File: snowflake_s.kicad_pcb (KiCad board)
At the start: 2 copper layers, 34.6 x 49.5 mm, 6 parts

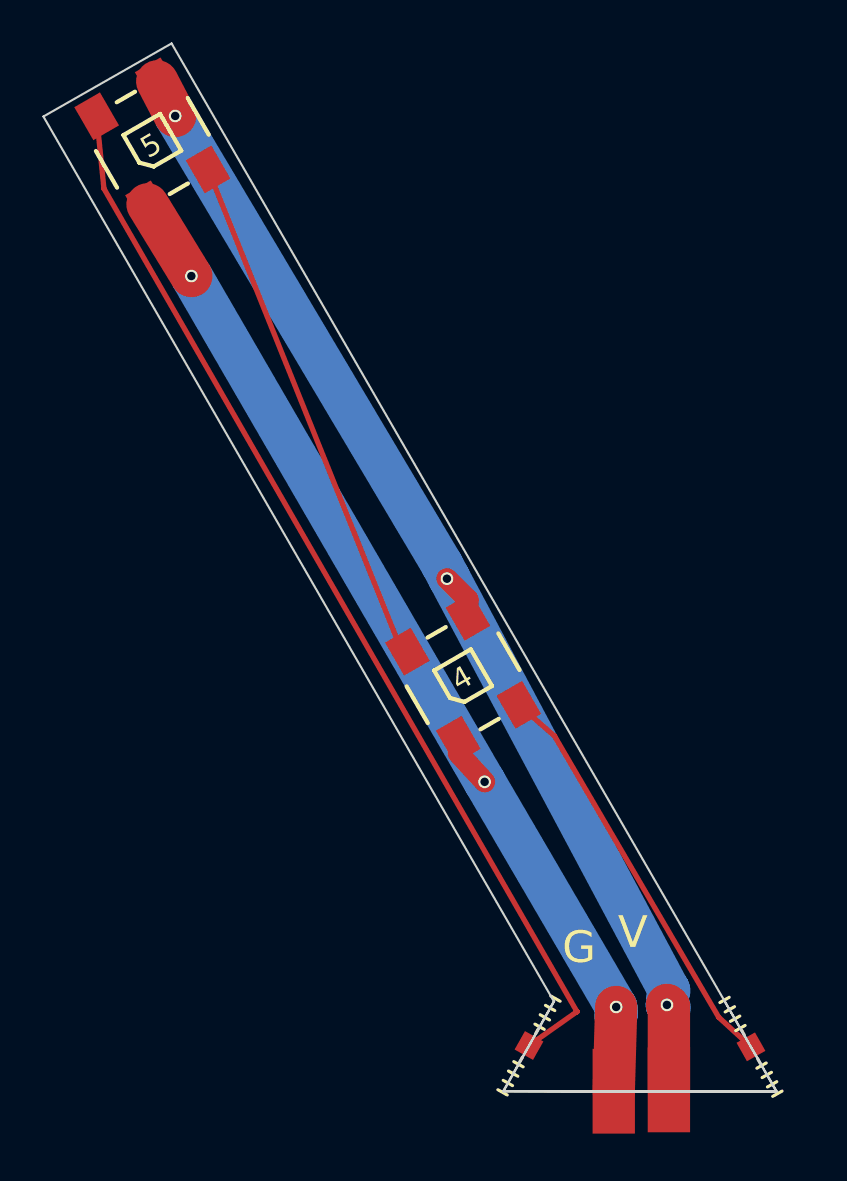
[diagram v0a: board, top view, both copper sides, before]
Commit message: reenable rotation
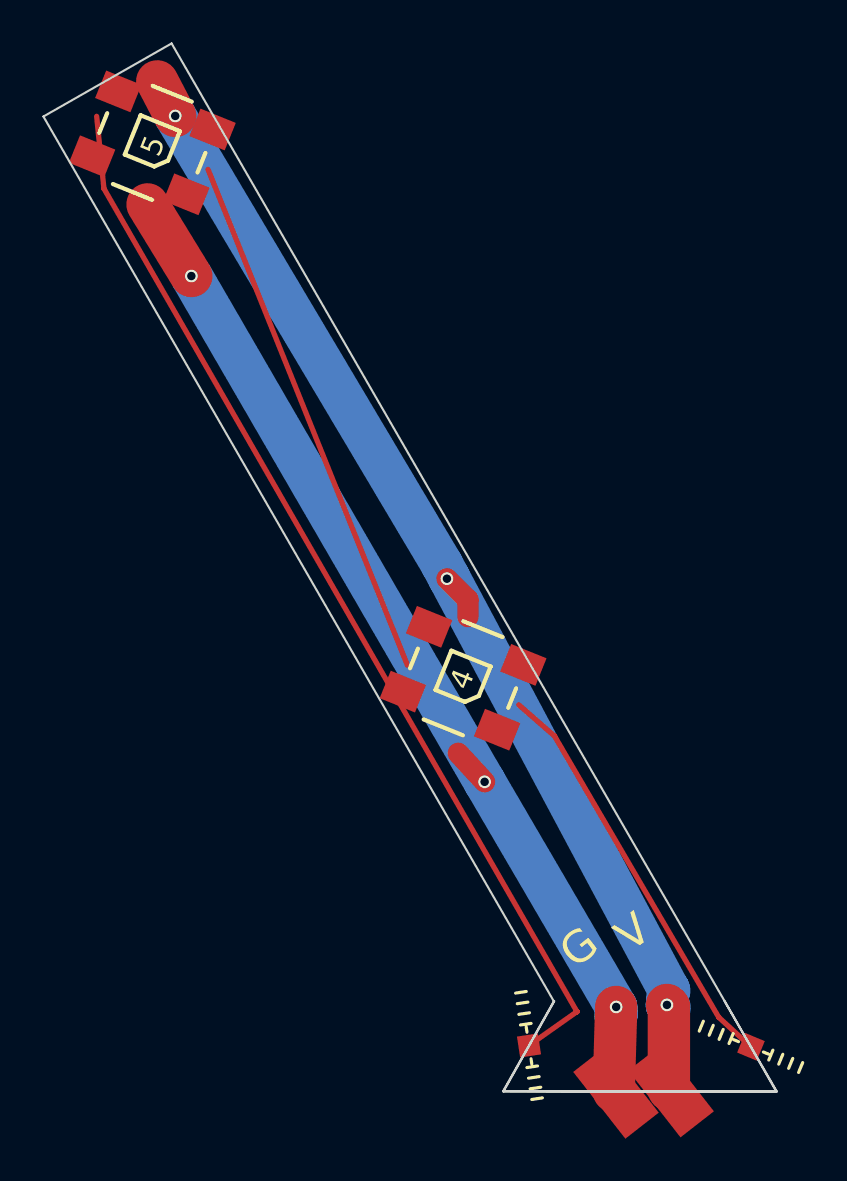
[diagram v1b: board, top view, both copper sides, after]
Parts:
- turned 4 to 68 degrees
- turned 5 to 68 degrees
- turned ? to 157.4 degrees
- turned ? to 278.6 degrees
- turned ? to 128 degrees (x2)
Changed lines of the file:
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@@
   )
   (module "Tiny Edge" (layer F.Cu)
-    (at 137.8585 101.473 119.4)
-    (fp_text reference "" (at 0 0.5 119.4) (layer F.SilkS)
-      (effects (font (size 1 1) (thickness 0.15)))
-    )
-    (fp_text value "" (at 3.175 -4.056 119.4) (layer F.Fab)
+    (at 137.8585 101.473 157.4)
+    (fp_text reference "" (at 0 0.5 157.4) (layer F.SilkS)
+      (effects (font (size 1 1) (thickness 0.15)))
+    )
+    (fp_text value "" (at 3.175 -4.056 157.4) (layer F.Fab)
       (effects (font (size 1 1) (thickness 0.15)))
     )
@@
     (fp_line (start -1.524 -0.254) (end -1.524 0.254) (layer F.SilkS) (width 0.15))
     (fp_line (start -1.016 -0.254) (end -1.016 0.254) (layer F.SilkS) (width 0.15))
-    (pad 1 smd rect (at 0 0 119.4) (size 1 1) (layers F.Cu F.Paste F.Mask))
+    (pad 1 smd rect (at 0 0 157.4) (size 1 1) (layers F.Cu F.Paste F.Mask))
   )
   (module "Tiny Edge" (layer F.Cu)
-    (at 127.381 101.4095 240.6)
-    (fp_text reference "" (at 0 0.5 240.6) (layer F.SilkS)
-      (effects (font (size 1 1) (thickness 0.15)))
-    )
-    (fp_text value "" (at 3.175 -4.056 240.6) (layer F.Fab)
+    (at 127.381 101.4095 278.6)
+    (fp_text reference "" (at 0 0.5 278.6) (layer F.SilkS)
+      (effects (font (size 1 1) (thickness 0.15)))
+    )
+    (fp_text value "" (at 3.175 -4.056 278.6) (layer F.Fab)
       (effects (font (size 1 1) (thickness 0.15)))
     )
@@
     (fp_line (start -1.524 -0.254) (end -1.524 0.254) (layer F.SilkS) (width 0.15))
     (fp_line (start -1.016 -0.254) (end -1.016 0.254) (layer F.SilkS) (width 0.15))
-    (pad 1 smd rect (at 0 0 240.6) (size 1 1) (layers F.Cu F.Paste F.Mask))
+    (pad 1 smd rect (at 0 0 278.6) (size 1 1) (layers F.Cu F.Paste F.Mask))
   )
   (module "Big pad" (layer F.Cu)
-    (at 134.112 103.378 90)
-    (fp_text reference "" (at 0.127 0.5 90) (layer F.SilkS)
-      (effects (font (size 1 1) (thickness 0.15)))
-    )
-    (fp_text value "" (at 0 -0.5 90) (layer F.Fab)
-      (effects (font (size 1 1) (thickness 0.15)))
-    )
-    (pad 1 smd rect (at -0.127 -0.127 90) (size 4 2) (layers F.Cu F.Paste F.Mask))
+    (at 134.112 103.378 128)
+    (fp_text reference "" (at 0.127 0.5 128) (layer F.SilkS)
+      (effects (font (size 1 1) (thickness 0.15)))
+    )
+    (fp_text value "" (at 0 -0.5 128) (layer F.Fab)
+      (effects (font (size 1 1) (thickness 0.15)))
+    )
+    (pad 1 smd rect (at -0.127 -0.127 128) (size 4 2) (layers F.Cu F.Paste F.Mask))
   )
   (module "Big pad" (layer F.Cu)
-    (at 131.5085 103.4415 90)
-    (fp_text reference "" (at 0.127 0.5 90) (layer F.SilkS)
-      (effects (font (size 1 1) (thickness 0.15)))
-    )
-    (fp_text value "" (at 0 -0.5 90) (layer F.Fab)
-      (effects (font (size 1 1) (thickness 0.15)))
-    )
-    (pad 1 smd rect (at -0.127 -0.127 90) (size 4 2) (layers F.Cu F.Paste F.Mask))
+    (at 131.5085 103.4415 128)
+    (fp_text reference "" (at 0.127 0.5 128) (layer F.SilkS)
+      (effects (font (size 1 1) (thickness 0.15)))
+    )
+    (fp_text value "" (at 0 -0.5 128) (layer F.Fab)
+      (effects (font (size 1 1) (thickness 0.15)))
+    )
+    (pad 1 smd rect (at -0.127 -0.127 128) (size 4 2) (layers F.Cu F.Paste F.Mask))
   )
   (module WS2812B:WS2812B (layer F.Cu)
-    (at 109.601 58.801 30)
-    (fp_text reference 5 (at -0.118493 0.078235 30) (layer F.SilkS)
-      (effects (font (size 1 1) (thickness 0.2)))
-    )
-    (fp_text value "" (at 0 4.8 30) (layer F.SilkS) hide
+    (at 109.601 58.801 68)
+    (fp_text reference 5 (at -0.118493 0.078235 68) (layer F.SilkS)
+      (effects (font (size 1 1) (thickness 0.2)))
+    )
+    (fp_text value "" (at 0 4.8 68) (layer F.SilkS) hide
       (effects (font (size 1 1) (thickness 0.2)))
     )
@@
     (fp_line (start 2.5 -2.5) (end 2.5 2.5) (layer Dwgs.User) (width 0.2))
     (fp_line (start -2.49936 2.49936) (end -2.49936 -2.49936) (layer Dwgs.User) (width 0.2))
-    (pad 1 smd rect (at 1.65 -2.4 30) (size 1.4 1.8) (layers F.Cu F.Paste F.Mask)
+    (pad 1 smd rect (at 1.65 -2.4 68) (size 1.4 1.8) (layers F.Cu F.Paste F.Mask)
       (net 1 /VCC))
-    (pad 2 smd rect (at -1.65 -2.4 30) (size 1.4 1.8) (layers F.Cu F.Paste F.Mask)
+    (pad 2 smd rect (at -1.65 -2.4 68) (size 1.4 1.8) (layers F.Cu F.Paste F.Mask)
       (net 5 "Net-(LED104-Pad4)"))
-    (pad 3 smd rect (at -1.65 2.4 30) (size 1.4 1.8) (layers F.Cu F.Paste F.Mask)
+    (pad 3 smd rect (at -1.65 2.4 68) (size 1.4 1.8) (layers F.Cu F.Paste F.Mask)
       (net 2 /GND))
-    (pad 4 smd rect (at 1.65 2.4 30) (size 1.4 1.8) (layers F.Cu F.Paste F.Mask)
+    (pad 4 smd rect (at 1.65 2.4 68) (size 1.4 1.8) (layers F.Cu F.Paste F.Mask)
       (net 3 "Net-(LED2-Pad4)"))
   )
   (module WS2812B:WS2812B (layer F.Cu)
-    (at 124.2695 84.074 30)
-    (fp_text reference 4 (at -0.054993 -0.03175 30) (layer F.SilkS)
-      (effects (font (size 1 1) (thickness 0.2)))
-    )
-    (fp_text value "" (at 0 4.8 30) (layer F.SilkS) hide
+    (at 124.2695 84.074 68)
+    (fp_text reference 4 (at -0.054993 -0.03175 68) (layer F.SilkS)
+      (effects (font (size 1 1) (thickness 0.2)))
+    )
+    (fp_text value "" (at 0 4.8 68) (layer F.SilkS) hide
       (effects (font (size 1 1) (thickness 0.2)))
     )
@@
     (fp_line (start 2.5 -2.5) (end 2.5 2.5) (layer Dwgs.User) (width 0.2))
     (fp_line (start -2.49936 2.49936) (end -2.49936 -2.49936) (layer Dwgs.User) (width 0.2))
-    (pad 1 smd rect (at 1.65 -2.4 30) (size 1.4 1.8) (layers F.Cu F.Paste F.Mask)
+    (pad 1 smd rect (at 1.65 -2.4 68) (size 1.4 1.8) (layers F.Cu F.Paste F.Mask)
       (net 1 /VCC))
-    (pad 2 smd rect (at -1.65 -2.4 30) (size 1.4 1.8) (layers F.Cu F.Paste F.Mask)
+    (pad 2 smd rect (at -1.65 -2.4 68) (size 1.4 1.8) (layers F.Cu F.Paste F.Mask)
       (net 3 "Net-(LED2-Pad4)"))
-    (pad 3 smd rect (at -1.65 2.4 30) (size 1.4 1.8) (layers F.Cu F.Paste F.Mask)
+    (pad 3 smd rect (at -1.65 2.4 68) (size 1.4 1.8) (layers F.Cu F.Paste F.Mask)
       (net 2 /GND))
-    (pad 4 smd rect (at 1.65 2.4 30) (size 1.4 1.8) (layers F.Cu F.Paste F.Mask)
+    (pad 4 smd rect (at 1.65 2.4 68) (size 1.4 1.8) (layers F.Cu F.Paste F.Mask)
       (net 4 "Net-(LED3-Pad4)"))
   )
-  (gr_text G (at 129.7432 96.774) (layer F.SilkS)
+  (gr_text G (at 129.7432 96.774 38) (layer F.SilkS)
     (effects (font (size 1.5 1.5) (thickness 0.3)))
   )
-  (gr_text V (at 132.2832 96.0628) (layer F.SilkS)
+  (gr_text V (at 132.2832 96.0628 38) (layer F.SilkS)
     (effects (font (size 1.5 1.5) (thickness 0.3)))
   )
@@
   (segment (start 124.498442 81.170539) (end 124.498442 80.365942) (width 1) (layer F.Cu) (net 1))
   (segment (start 124.498442 80.365942) (end 123.5075 79.375) (width 1) (layer F.Cu) (net 1))
-  (via (at 123.5075 79.375) (size 0.6) (drill 0.4) (layers F.Cu B.Cu) (net 1))
+  (via (at 123.5075 79.375 38) (size 0.6) (drill 0.4) (layers F.Cu B.Cu) (net 1))
   (segment (start 123.5075 79.375) (end 123.558389 79.324111) (width 1) (layer B.Cu) (net 1))
   (segment (start 123.558389 79.324111) (end 123.602932 79.324111) (width 1) (layer B.Cu) (net 1))
-  (via (at 133.892471 99.494435) (size 0.6) (drill 0.4) (layers F.Cu B.Cu) (net 1))
+  (via (at 133.892471 99.494435 38) (size 0.6) (drill 0.4) (layers F.Cu B.Cu) (net 1))
   (segment (start 133.985 99.586964) (end 133.892471 99.494435) (width 2) (layer F.Cu) (net 1))
   (segment (start 133.892471 99.494435) (end 133.971455 98.768191) (width 2) (layer B.Cu) (net 1))
@@
   (segment (start 123.602932 79.324111) (end 123.267884 78.695796) (width 2) (layer B.Cu) (net 1))
   (segment (start 123.267884 78.695796) (end 110.6805 57.531) (width 2) (layer B.Cu) (net 1))
-  (via (at 110.6805 57.531) (size 0.6) (drill 0.4) (layers F.Cu B.Cu) (net 1))
+  (via (at 110.6805 57.531 38) (size 0.6) (drill 0.4) (layers F.Cu B.Cu) (net 1))
   (segment (start 110.6805 57.531) (end 109.829942 55.897539) (width 2) (layer F.Cu) (net 1) (status 20))
   (segment (start 131.5085 99.8855) (end 131.495605 99.590527) (width 2) (layer B.Cu) (net 2))
-  (via (at 131.495605 99.590527) (size 0.6) (drill 0.4) (layers F.Cu B.Cu) (net 2))
+  (via (at 131.495605 99.590527 38) (size 0.6) (drill 0.4) (layers F.Cu B.Cu) (net 2))
   (segment (start 131.495605 99.590527) (end 131.3815 103.5685) (width 2) (layer F.Cu) (net 2))
   (segment (start 131.495605 99.590527) (end 131.5085 99.8855) (width 2) (layer B.Cu) (net 2))
@@
   (segment (start 109.372058 61.704461) (end 111.4425 65.0875) (width 2) (layer F.Cu) (net 2) (status 10))
   (segment (start 111.4425 65.0875) (end 125.2855 88.9635) (width 2) (layer B.Cu) (net 2))
-  (via (at 111.4425 65.0875) (size 0.6) (drill 0.4) (layers F.Cu B.Cu) (net 2))
+  (via (at 111.4425 65.0875 38) (size 0.6) (drill 0.4) (layers F.Cu B.Cu) (net 2))
   (segment (start 125.2855 88.9635) (end 124.040558 87.612461) (width 1) (layer F.Cu) (net 2) (status 20))
-  (via (at 125.2855 88.9635) (size 0.6) (drill 0.4) (layers F.Cu B.Cu) (net 2))
+  (via (at 125.2855 88.9635 38) (size 0.6) (drill 0.4) (layers F.Cu B.Cu) (net 2))
   (segment (start 121.640558 83.455539) (end 112.229942 60.054461) (width 0.25) (layer F.Cu) (net 3) (status 10))
   (segment (start 136.3345 100.076) (end 137.8585 101.473) (width 0.25) (layer F.Cu) (net 4))
